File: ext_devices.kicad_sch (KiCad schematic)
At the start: 9 parts

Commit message: moved LEDs to separate sheet as there's gonna be many; experimented with buses
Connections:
- net I2C1_SCL renamed I2C_SCL
- net I2C1_SDA renamed I2C_SDA
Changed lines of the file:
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@@
-    )
-  )
-  (global_label "I2C1_SDA" (shape input) (at 43.815 149.86 180) (fields_autoplaced)
-    (effects (font (size 1.27 1.27)) (justify right))
-    (property "Intersheet References" "${INTERSHEET_REFS}" (id 0) (at 32.5724 149.9394 0)
-      (effects (font (size 1.27 1.27)) (justify right) hide)
     )
   )
@@
     )
   )
-  (global_label "I2C1_SCL" (shape input) (at 43.815 154.94 180) (fields_autoplaced)
-    (effects (font (size 1.27 1.27)) (justify right))
-    (property "Intersheet References" "${INTERSHEET_REFS}" (id 0) (at 32.6329 155.0194 0)
-      (effects (font (size 1.27 1.27)) (justify right) hide)
-    )
-  )
   (global_label "ARDUINO_D7" (shape input) (at 135.255 50.8 180) (fields_autoplaced)
     (effects (font (size 1.27 1.27)) (justify right))
@@
     (effects (font (size 1.27 1.27)) (justify right))
   )
+  (hierarchical_label "I2C_SDA" (shape input) (at 43.815 149.86 180)
+    (effects (font (size 1.27 1.27)) (justify right))
+  )
   (hierarchical_label "+5V_EXT" (shape input) (at 95.885 82.55 0)
     (effects (font (size 1.27 1.27)) (justify left))
@@
     (effects (font (size 1.27 1.27)) (justify left))
   )
+  (hierarchical_label "I2C_SCL" (shape input) (at 43.815 154.94 180)
+    (effects (font (size 1.27 1.27)) (justify right))
+  )
   (hierarchical_label "+5V_EXT" (shape input) (at 135.255 87.63 180)
     (effects (font (size 1.27 1.27)) (justify right))
@@
   (symbol (lib_id "power:+3.3V") (at 51.435 129.54 0) (unit 1)
     (in_bom yes) (on_board yes) (fields_autoplaced)
-    (property "Reference" "#PWR?" (id 0) (at 51.435 133.35 0)
+    (property "Reference" "#PWR0178" (id 0) (at 51.435 133.35 0)
       (effects (font (size 1.27 1.27)) hide)
     )
@@
   (symbol (lib_id "power:GND") (at 187.325 95.25 0) (unit 1)
     (in_bom yes) (on_board yes) (fields_autoplaced)
-    (property "Reference" "#PWR?" (id 0) (at 187.325 101.6 0)
+    (property "Reference" "#PWR0176" (id 0) (at 187.325 101.6 0)
       (effects (font (size 1.27 1.27)) hide)
     )
@@
   (symbol (lib_id "power:GND") (at 57.785 87.63 0) (unit 1)
     (in_bom yes) (on_board yes) (fields_autoplaced)
-    (property "Reference" "#PWR?" (id 0) (at 57.785 93.98 0)
+    (property "Reference" "#PWR0185" (id 0) (at 57.785 93.98 0)
       (effects (font (size 1.27 1.27)) hide)
     )
@@
   (symbol (lib_id "power:GND") (at 41.275 135.89 0) (unit 1)
     (in_bom yes) (on_board yes) (fields_autoplaced)
-    (property "Reference" "#PWR?" (id 0) (at 41.275 142.24 0)
+    (property "Reference" "#PWR0179" (id 0) (at 41.275 142.24 0)
       (effects (font (size 1.27 1.27)) hide)
     )
@@
   (symbol (lib_id "power:GND") (at 53.975 165.1 0) (unit 1)
     (in_bom yes) (on_board yes) (fields_autoplaced)
-    (property "Reference" "#PWR?" (id 0) (at 53.975 171.45 0)
+    (property "Reference" "#PWR0180" (id 0) (at 53.975 171.45 0)
       (effects (font (size 1.27 1.27)) hide)
     )
@@
   (symbol (lib_id "power:GND") (at 113.665 38.1 0) (unit 1)
     (in_bom yes) (on_board yes) (fields_autoplaced)
-    (property "Reference" "#PWR?" (id 0) (at 113.665 44.45 0)
+    (property "Reference" "#PWR0184" (id 0) (at 113.665 44.45 0)
       (effects (font (size 1.27 1.27)) hide)
     )
@@
   (symbol (lib_id "power:GND") (at 66.675 135.89 0) (unit 1)
     (in_bom yes) (on_board yes) (fields_autoplaced)
-    (property "Reference" "#PWR?" (id 0) (at 66.675 142.24 0)
+    (property "Reference" "#PWR0177" (id 0) (at 66.675 142.24 0)
       (effects (font (size 1.27 1.27)) hide)
     )
@@
   (symbol (lib_id "power:GND") (at 95.885 87.63 0) (unit 1)
     (in_bom yes) (on_board yes) (fields_autoplaced)
-    (property "Reference" "#PWR?" (id 0) (at 95.885 93.98 0)
+    (property "Reference" "#PWR0182" (id 0) (at 95.885 93.98 0)
       (effects (font (size 1.27 1.27)) hide)
     )
@@
   (symbol (lib_id "power:GND") (at 113.665 92.71 0) (unit 1)
     (in_bom yes) (on_board yes) (fields_autoplaced)
-    (property "Reference" "#PWR?" (id 0) (at 113.665 99.06 0)
+    (property "Reference" "#PWR0181" (id 0) (at 113.665 99.06 0)
       (effects (font (size 1.27 1.27)) hide)
     )
@@
   (symbol (lib_id "power:GND") (at 113.665 74.93 0) (unit 1)
     (in_bom yes) (on_board yes) (fields_autoplaced)
-    (property "Reference" "#PWR?" (id 0) (at 113.665 81.28 0)
-      (effects (font (size 1.27 1.27)) hide)
-    )
+    (property "Reference" "#PWR0183" (id 0) (at 113.665 81.28 0)
+      (effects (font (size 1.27 1.27)) hide)
+    )

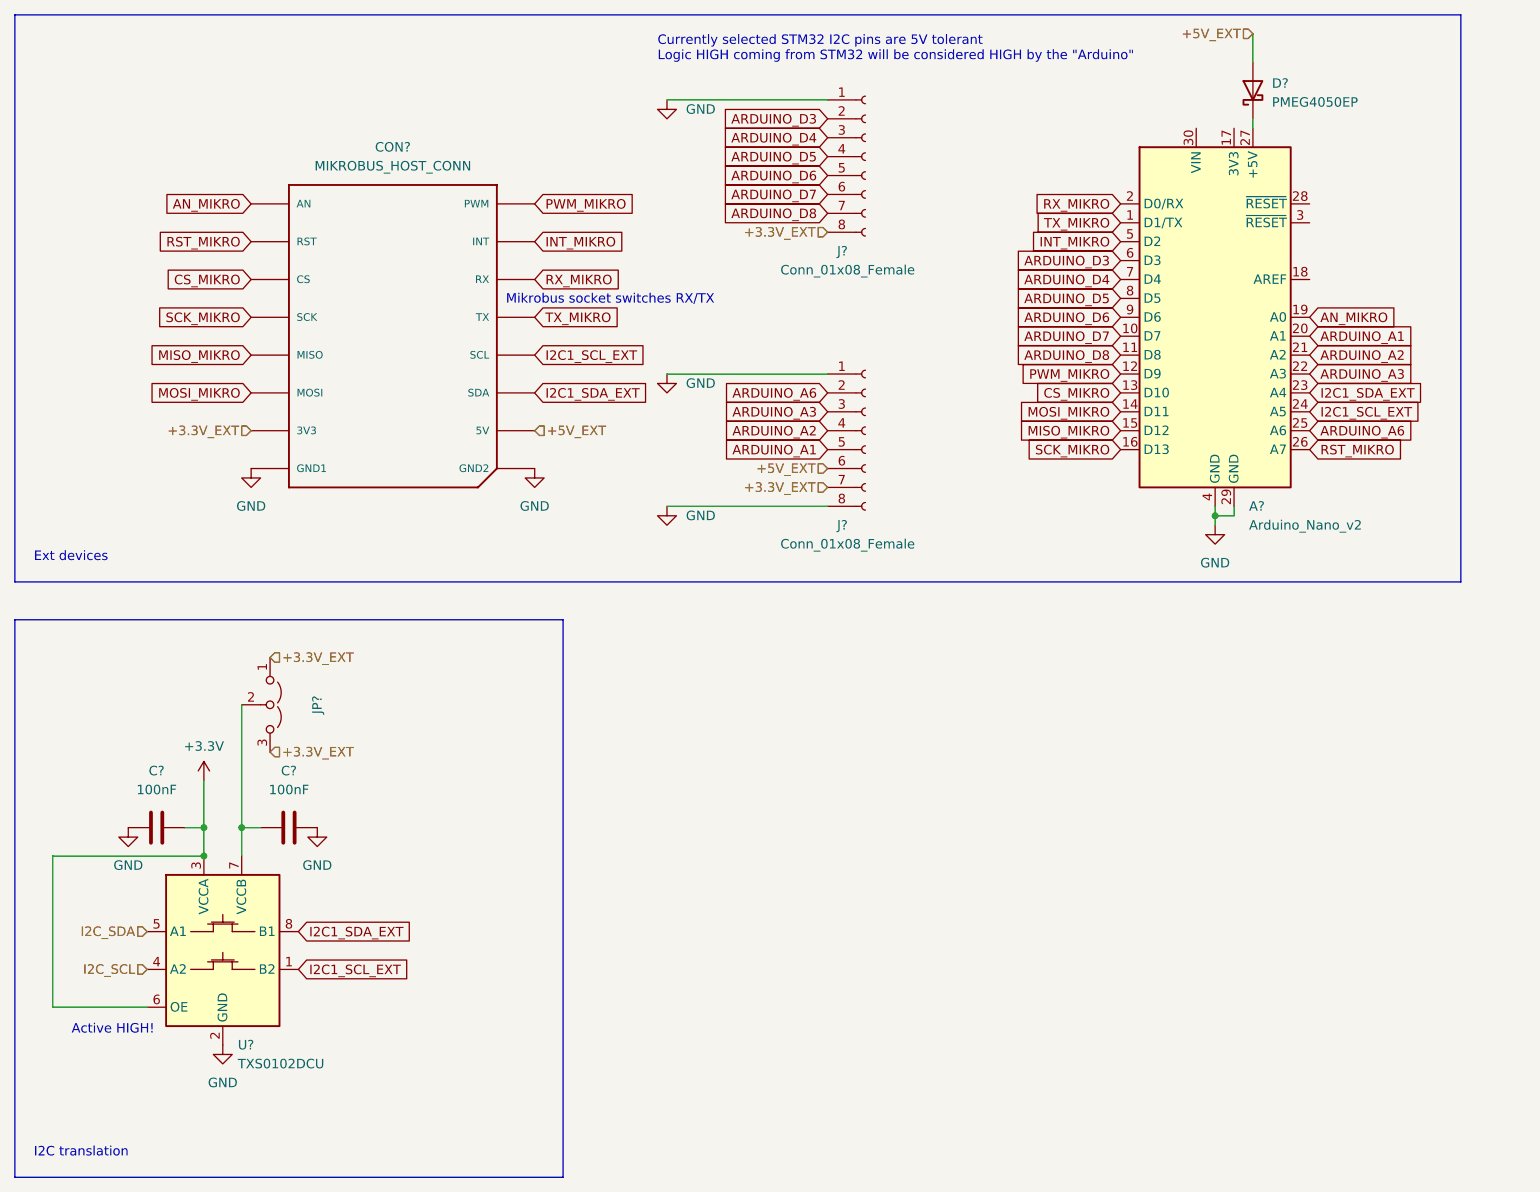
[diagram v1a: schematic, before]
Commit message: annotated all schematics, modified ext_devices
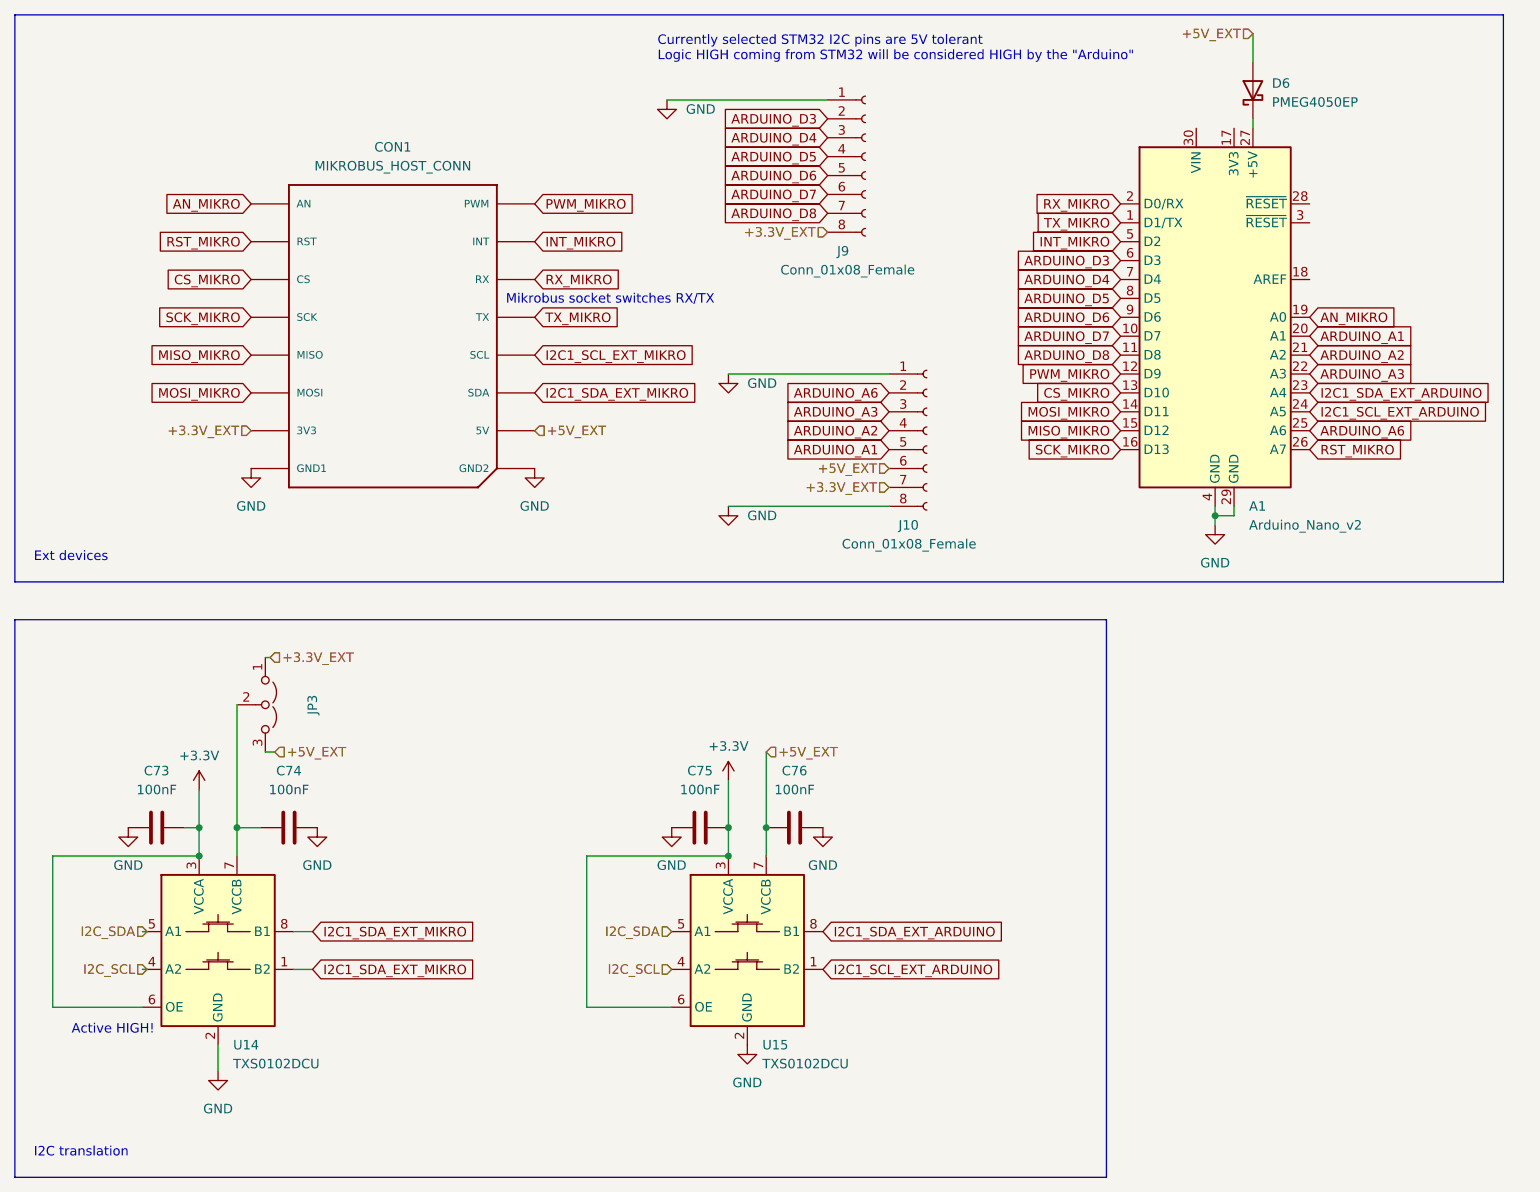
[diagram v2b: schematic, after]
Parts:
- added C75, C76: 100nF, Capacitor_SMD:C_0805_2012Metric_Pad1.18x1.45mm_HandSolder, symbol Device:C
- added U15: TXS0102DCU, Package_SO:VSSOP-8_2.3x2mm_P0.5mm, symbol Logic_LevelTranslator:TXS0102DCU
- gave numbers to parts that had none: 9
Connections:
- net +3.3V_EXT: no longer JP3.3 (B)
- net +3V3: now also C75.2, U15.3 (VCCA), U15.6 (OE)
- net +5V_EXT: now also JP3.3 (B), C76.1, U15.7 (VCCB)
- net GND: now also C75.1, C76.2, U15.2 (GND)
- net I2C_SCL: now also U15.4 (A2)
- net I2C_SDA: now also U15.5 (A1)
- removed net I2C1_SCL_EXT: A1.24 (A5), CON1.P12 (SCL), U14.1 (B2)
- net I2C1_SDA_EXT renamed I2C1_SDA_EXT_MIKRO
- net I2C1_SDA_EXT_MIKRO: now also U14.1 (B2); no longer A1.23 (A4)
- new net I2C1_SCL_EXT_ARDUINO: A1.24 (A5), U15.1 (B2)
- new net I2C1_SCL_EXT_MIKRO: CON1.P12 (SCL)
- new net I2C1_SDA_EXT_ARDUINO: A1.23 (A4), U15.8 (B1)
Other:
- moved on the sheet: J10, JP3, U14
